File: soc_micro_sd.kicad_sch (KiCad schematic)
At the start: 11 parts, among them J4 Micro_SD_Card_Det2, U2 Allwinner_V3S

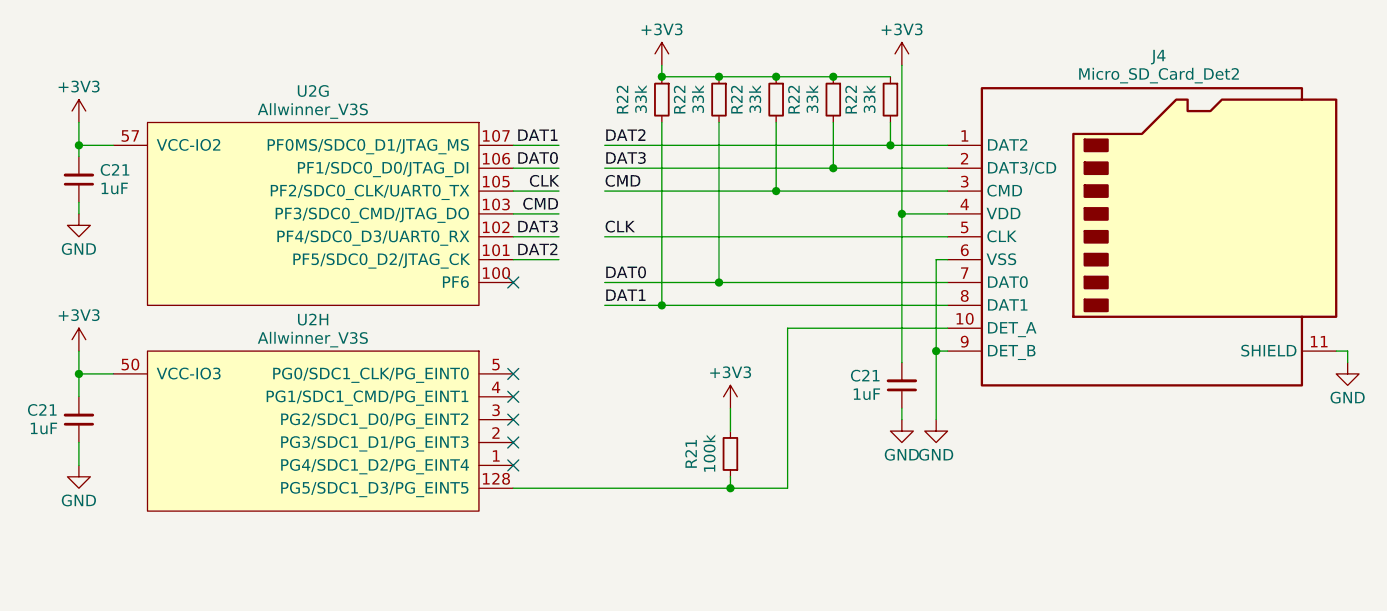
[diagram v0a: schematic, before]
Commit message: Finish routing for the most part
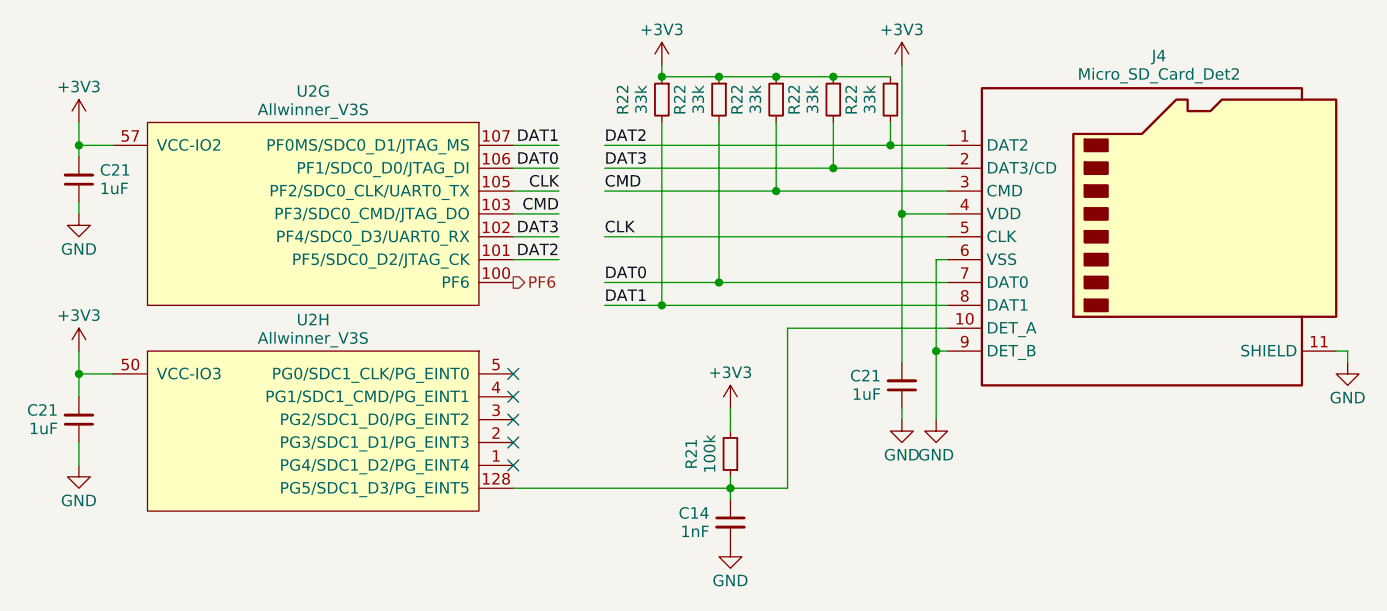
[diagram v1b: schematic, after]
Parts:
- added C14: 1nF, Capacitor_SMD:C_0402_1005Metric, symbol Device:C_Small
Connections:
- net GND: now also C14.2
- net PF6: now reaches U2.100 (PF6)
- net at J4.10 (DET_A), R21.1, U2.128 (PG5/SDC1_D3/PG_EINT5): now also C14.1
- no-connect marks 6 -> 5
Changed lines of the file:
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@@
   )
   (no_connect (at 74.93 88.9))
-  (no_connect (at 74.93 68.58))
   (no_connect (at 74.93 78.74))
   (no_connect (at 74.93 81.28))
@@
     (stroke (width 0) (type default))
   )
+  (wire (pts (xy 99.06 91.44) (xy 99.06 92.71))
+    (stroke (width 0) (type default))
+  )
   (wire (pts (xy 74.93 66.04) (xy 80.01 66.04))
     (stroke (width 0) (type default))
@@
   (label "DAT0" (at 80.01 55.88 180) (fields_autoplaced)
     (effects (font (size 1.27 1.27)) (justify right bottom))
+  )
+  (hierarchical_label "PF6" (shape output) (at 74.93 68.58 0) (fields_autoplaced)
+    (effects (font (size 1.27 1.27)) (justify left))
   )
   (symbol (lib_id "Device:R_Small") (at 116.84 48.26 0) (mirror y) (unit 1)
@@
     )
   )
+  (symbol (lib_id "Device:C_Small") (at 99.06 95.25 0) (mirror y) (unit 1)
+    (in_bom yes) (on_board yes) (dnp no)
+    (property "Reference" "C14" (at 96.7359 94.2323 0)
+      (effects (font (size 1.27 1.27)) (justify left))
+    )
+    (property "Value" "1nF" (at 96.7359 96.2803 0)
+      (effects (font (size 1.27 1.27)) (justify left))
+    )
+    (property "Footprint" "Capacitor_SMD:C_0402_1005Metric" (at 99.06 95.25 0)
+      (effects (font (size 1.27 1.27)) hide)
+    )
+    (property "Datasheet" "~" (at 99.06 95.25 0)
+      (effects (font (size 1.27 1.27)) hide)
+    )
+    (property "LCSC" "C1523" (at 99.06 95.25 0)
+      (effects (font (size 1.27 1.27)) hide)
+    )
+    (pin "1")
+    (pin "2")
+    (instances
+      (project "OpenHomeSwitch"
+        (path "/1d58c53f-167c-46c6-b61a-0c5d76c66e31/71e1ec36-fcc5-4ea9-a9bb-92fd21a85ab0/fcbac710-5c4c-4f73-a659-520d2a4da378"
+          (reference "C14") (unit 1)
+        )
+        (path "/1d58c53f-167c-46c6-b61a-0c5d76c66e31/41bdf90a-7af2-4b3b-98f6-50835501a67f/c84b2009-868a-4c9e-aa94-eb599aafac16"
+          (reference "C103") (unit 1)
+        )
+      )
+    )
+  )
   (symbol (lib_id "Device:C_Small") (at 26.67 83.82 0) (mirror x) (unit 1)
     (in_bom yes) (on_board yes) (dnp no)
@@
         )
       )
+    )
+  )
+  (symbol (lib_id "power:GND") (at 99.06 97.79 0) (unit 1)
+    (in_bom yes) (on_board yes) (dnp no) (fields_autoplaced)
+    (property "Reference" "#PWR011" (at 99.06 104.14 0)
+      (effects (font (size 1.27 1.27)) hide)
+    )
+    (property "Value" "GND" (at 99.06 101.735 0)
+      (effects (font (size 1.27 1.27)))
+    )
+    (property "Footprint" "" (at 99.06 97.79 0)
+      (effects (font (size 1.27 1.27)) hide)
+    )
+    (property "Datasheet" "" (at 99.06 97.79 0)
+      (effects (font (size 1.27 1.27)) hide)
+    )
+    (pin "1")
+    (instances
+      (project "OpenHomeSwitch"
+        (path "/1d58c53f-167c-46c6-b61a-0c5d76c66e31/41bdf90a-7af2-4b3b-98f6-50835501a67f/c84b2009-868a-4c9e-aa94-eb599aafac16"
+          (reference "#PWR011") (unit 1)
+        )
+      )

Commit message: Add V3s variant with smaller exposed GND pad
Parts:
- U2: footprint Package_QFP_Allwinner:LQFP-128_14x14mm_P0.4mm_EPAD_8x8mm -> Package_QFP_Allwinner:LQFP-128_14x14mm_P0.4mm_EPAD_5.72x5.72mm
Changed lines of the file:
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@@
       (effects (font (size 1.27 1.27)))
     )
-    (property "Footprint" "Package_QFP_Allwinner:LQFP-128_14x14mm_P0.4mm_EPAD_8x8mm" (at 81.28 81.28 0)
+    (property "Footprint" "Package_QFP_Allwinner:LQFP-128_14x14mm_P0.4mm_EPAD_5.72x5.72mm" (at 81.28 81.28 0)
       (effects (font (size 1.27 1.27)) hide)
     )
@@
       (effects (font (size 1.27 1.27)))
     )
-    (property "Footprint" "Package_QFP_Allwinner:LQFP-128_14x14mm_P0.4mm_EPAD_8x8mm" (at 86.36 106.68 0)
-      (effects (font (size 1.27 1.27)) hide)
-    )
+    (property "Footprint" "Package_QFP_Allwinner:LQFP-128_14x14mm_P0.4mm_EPAD_5.72x5.72mm" (at 86.36 106.68 0)
+      (effects (font (size 1.27 1.27)) hide)
+    )

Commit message: Fix LCSC part numbers
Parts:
- U2: LCSC (none) -> C2687449
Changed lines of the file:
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@@
+      (effects (font (size 1.27 1.27)) hide)
+    )
+    (property "LCSC" "C2687449" (at 53.34 50.8 0)
       (effects (font (size 1.27 1.27)) hide)
     )
@@
       (effects (font (size 1.27 1.27)) hide)
     )
+    (property "LCSC" "C2687449" (at 58.42 76.2 0)
+      (effects (font (size 1.27 1.27)) hide)
+    )
